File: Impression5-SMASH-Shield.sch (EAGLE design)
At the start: 113 parts, among them IC1 7805TV, J1 1725656, J10 61300811121, J11 61300811121, J12 61300611121, J13 61300311121, J14 61300311121, J15 61300311121, J16 61300311121, J17 61300311121, J18 61300311121, J19 61300611121, J2 1725656, J20 61300311121, J21 61300311121, J22 61300411121, J23 61300311121, J24 61300311121, J25 61300311121, J26 61300311121, J27 61300311121, J28 61300311121, J29 61300311121, J3 1725656, J30 61300311121, J31 61300311121, J32 61300311121, J33 61300311121, J34 61300311121, J35 61300311121, J36 61300311121, J37 61300311121, J38 61300311121, J39 61300311121, J4 1725656, J40 61300311121, J41 61300311121, J42 61300311121, J43 61300211121, J44 61300211121, J45 61300211121, J46 61300211121, J47 61300811121, J48 61300311121, J49 61300311121, J5 1725656, J50 61300311121, J51 61300311121, J52 61300611121, J53 61300811121, J54 61300811121, J6 1725656, J7 1725656, J8 1725656, J9 1725656, Q1 IRF512, Q2 IRF512, Q3 IRF512, Q4 IRF512, Q5 IRF512, Q6 IRF512, Q7 IRF512, Q8 IRF512

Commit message: Changed the Order of the Text to better line up the LM317 Programming Resistors.
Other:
- note added: "Small Vout = 3V6 R17 = 243R R16 = 453R Vout = 2.0V R19 = 243R R18 = 147R"
- note removed: "Small Vout = 2.0V R19 = 243R R18 = 147R Vout = 3V6 R17 = 243R R16 = 453R"
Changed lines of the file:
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@@
 R18 = 536R</text>
 <text x="182.88" y="73.66" size="1.778" layer="91">Small
+Vout = 3V6
+R17 = 243R
+R16 = 453R
 Vout = 2.0V
 R19 = 243R
-R18 = 147R
-Vout = 3V6
-R17 = 243R
-R16 = 453R</text>
+R18 = 147R</text>
 </plain>
 <instances>

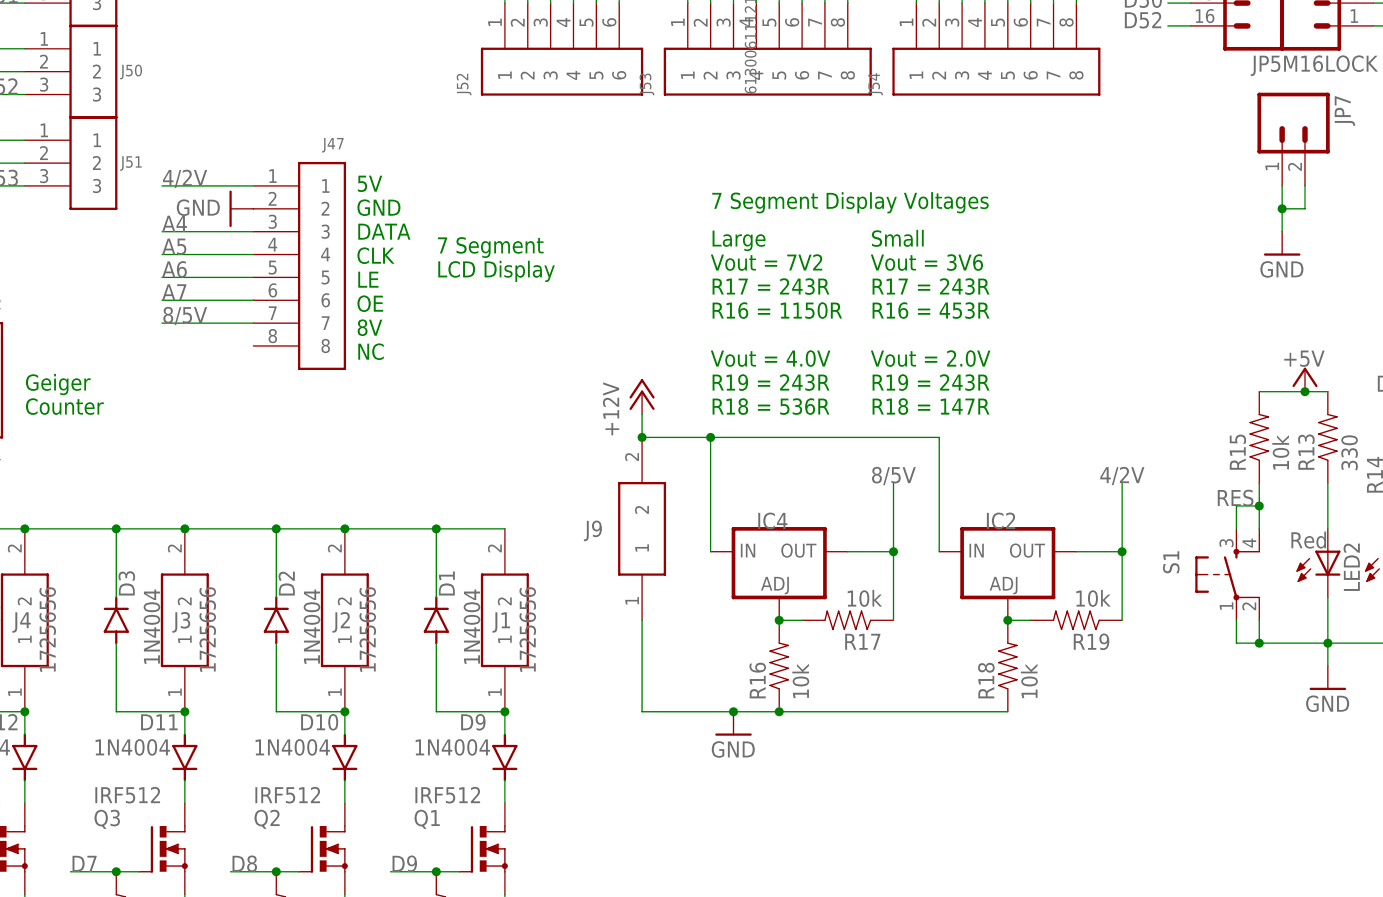
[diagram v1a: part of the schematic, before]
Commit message: changed 4/2V to 5VL. This powers the VDD of the TLC5917 and needs to be 5V.
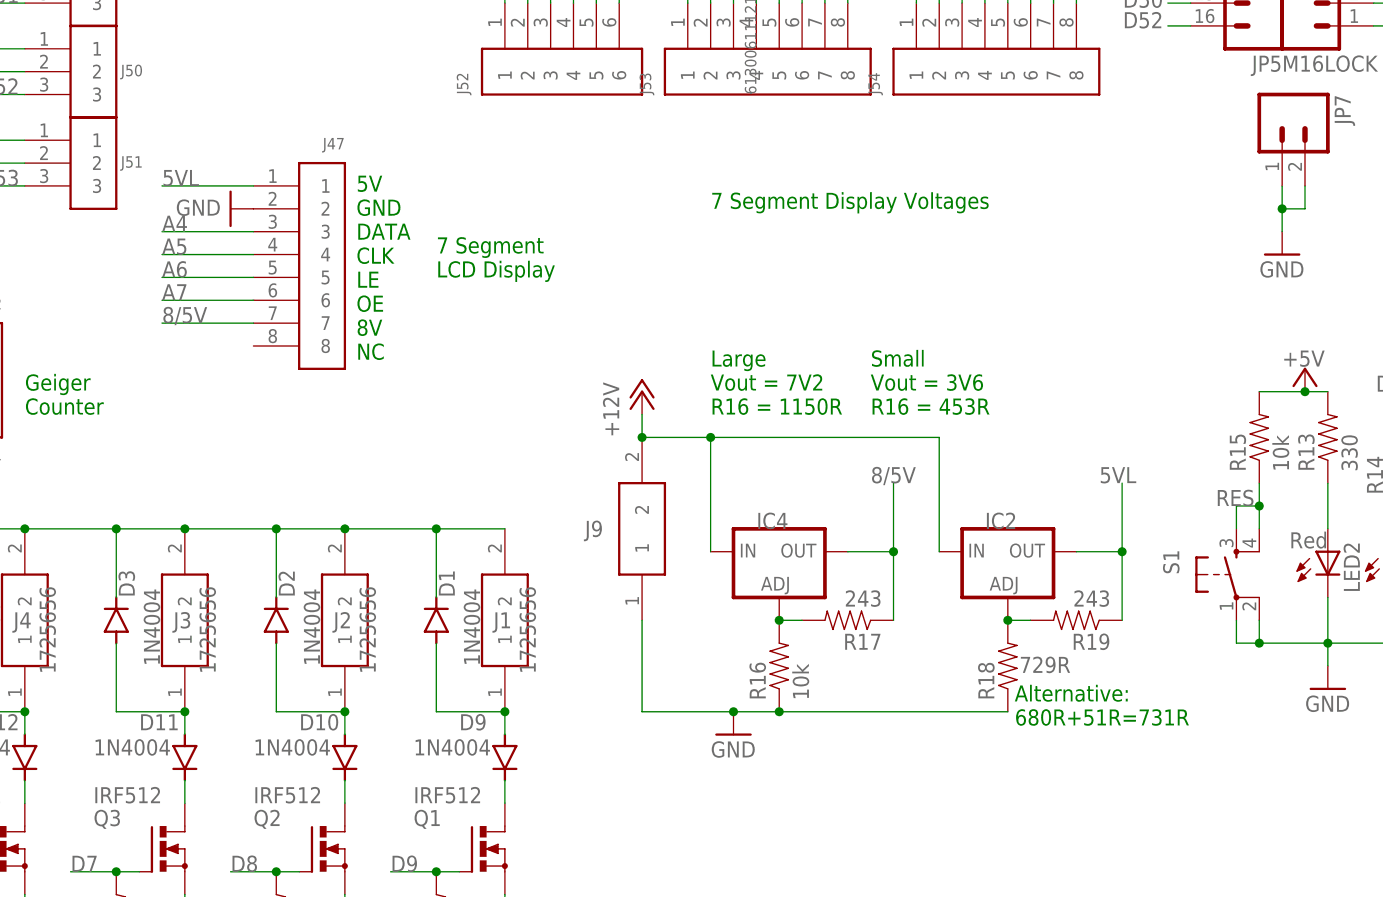
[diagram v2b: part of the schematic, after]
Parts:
- R17, R19: value 10k -> 243
- R18: value 10k -> 729R
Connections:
- net 4/2V renamed 5VL
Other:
- note added: "Alternative: 680R+51R=731R"
- note added: "Large Vout = 7V2 R16 = 1150R"
- note added: "Small Vout = 3V6 R16 = 453R"
- note removed: "Large Vout = 7V2 R17 = 243R R16 = 1150R Vout = 4.0V R19 = 243R R18 = 536R"
- note removed: "Small Vout = 3V6 R17 = 243R R16 = 453R Vout = 2.0V R19 = 243R R18 = 147R"
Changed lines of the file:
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@@
 <part name="IC4" library="v-reg" library_urn="urn:adsk.eagle:library:409" deviceset="LM317TS" device="" package3d_urn="urn:adsk.eagle:package:30353/1"/>
 <part name="R16" library="SparkFun" deviceset="RESISTOR" device="PTH1" value="10k"/>
-<part name="R17" library="SparkFun" deviceset="RESISTOR" device="PTH1" value="10k"/>
+<part name="R17" library="SparkFun" deviceset="RESISTOR" device="PTH1" value="243"/>
 <part name="IC2" library="v-reg" library_urn="urn:adsk.eagle:library:409" deviceset="LM317TS" device="" package3d_urn="urn:adsk.eagle:package:30353/1"/>
-<part name="R18" library="SparkFun" deviceset="RESISTOR" device="PTH1" value="10k"/>
-<part name="R19" library="SparkFun" deviceset="RESISTOR" device="PTH1" value="10k"/>
+<part name="R18" library="SparkFun" deviceset="RESISTOR" device="PTH1" value="729R"/>
+<part name="R19" library="SparkFun" deviceset="RESISTOR" device="PTH1" value="243"/>
 </parts>
 <sheets>
@@
 <text x="165.1" y="73.66" size="1.778" layer="91">Large
 Vout = 7V2
-R17 = 243R
-R16 = 1150R
-Vout = 4.0V
-R19 = 243R
-R18 = 536R</text>
+R16 = 1150R</text>
 <text x="182.88" y="73.66" size="1.778" layer="91">Small
 Vout = 3V6
-R17 = 243R
-R16 = 453R
-Vout = 2.0V
-R19 = 243R
-R18 = 147R</text>
+R16 = 453R</text>
+<text x="198.882" y="39.116" size="1.778" layer="91">Alternative:
+680R+51R=731R</text>
 </plain>
 <instances>
@@
 <instance part="R18" gate="G$1" x="198.12" y="45.72" smashed="yes" rot="R90">
 <attribute name="NAME" x="196.6214" y="41.91" size="1.778" layer="95" rot="R90"/>
-<attribute name="VALUE" x="201.422" y="41.91" size="1.778" layer="96" rot="R90"/>
+<attribute name="VALUE" x="199.39" y="44.958" size="1.778" layer="96"/>
 </instance>
 <instance part="R19" gate="G$1" x="205.74" y="50.8" smashed="yes" rot="R180">
@@
 </segment>
 </net>
-<net name="4/2V" class="0">
+<net name="5VL" class="0">
 <segment>
 <label x="208.28" y="66.04" size="1.778" layer="95"/>

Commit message: Changed the 8/5V to 9/5V, actually 9V2 and 5V0 respectively. These voltages needs to provide the maximum Vf that the 7-Segments may need. The max Vf are: SA23-11SRWA = 9.2V SA15-11EWA  = 5.0V
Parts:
- R16: value 10k -> 1551R or 729R
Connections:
- net 8/5V renamed 9/5V
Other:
- note added: "Alternative: 1500R+51R=1551R 680R+51R=731R"
- note added: "Large Vout = 9V2 R16 = 1551R"
- note added: "Small Vout = 5V0 R16 = 729R"
- note removed: "Large Vout = 7V2 R16 = 1150R"
- note removed: "Small Vout = 3V6 R16 = 453R"
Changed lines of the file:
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@@
 <part name="R12" library="SparkFun" deviceset="RESISTOR" device="PTH1" value="10k"/>
 <part name="IC4" library="v-reg" library_urn="urn:adsk.eagle:library:409" deviceset="LM317TS" device="" package3d_urn="urn:adsk.eagle:package:30353/1"/>
-<part name="R16" library="SparkFun" deviceset="RESISTOR" device="PTH1" value="10k"/>
+<part name="R16" library="SparkFun" deviceset="RESISTOR" device="PTH1" value="1551R or 729R"/>
 <part name="R17" library="SparkFun" deviceset="RESISTOR" device="PTH1" value="243"/>
 <part name="IC2" library="v-reg" library_urn="urn:adsk.eagle:library:409" deviceset="LM317TS" device="" package3d_urn="urn:adsk.eagle:package:30353/1"/>
@@
 <text x="165.1" y="96.52" size="1.778" layer="91">7 Segment Display Voltages</text>
 <text x="165.1" y="73.66" size="1.778" layer="91">Large
-Vout = 7V2
-R16 = 1150R</text>
+Vout = 9V2
+R16 = 1551R</text>
 <text x="182.88" y="73.66" size="1.778" layer="91">Small
-Vout = 3V6
-R16 = 453R</text>
+Vout = 5V0
+R16 = 729R</text>
 <text x="198.882" y="39.116" size="1.778" layer="91">Alternative:
+680R+51R=731R</text>
+<text x="173.736" y="33.274" size="1.778" layer="91">Alternative:
+1500R+51R=1551R
 680R+51R=731R</text>
 </plain>
@@
 <instance part="R16" gate="G$1" x="172.72" y="45.72" smashed="yes" rot="R90">
 <attribute name="NAME" x="171.2214" y="41.91" size="1.778" layer="95" rot="R90"/>
-<attribute name="VALUE" x="176.022" y="41.91" size="1.778" layer="96" rot="R90"/>
+<attribute name="VALUE" x="173.99" y="42.418" size="1.778" layer="96"/>
 </instance>
 <instance part="R17" gate="G$1" x="180.34" y="50.8" smashed="yes" rot="R180">
@@
 </segment>
 </net>
-<net name="8/5V" class="0">
+<net name="9/5V" class="0">
 <segment>
 <label x="182.88" y="66.04" size="1.778" layer="95"/>

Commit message: Added Notes for double use of D2 and D9
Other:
- note added: "Note - D2 is used in TWO places, on J8 Mosfet control and Geiger Counter Pulse Interupt D9 is used in TWO places, on J1 Mosfet control and Relay Board control"
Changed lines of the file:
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@@
 <text x="88.9" y="73.66" size="1.778" layer="91">Geiger
 Counter</text>
-<text x="165.1" y="96.52" size="1.778" layer="91">7 Segment Display Voltages</text>
+<text x="160.02" y="81.28" size="1.778" layer="91">7 Segment Display Voltages</text>
 <text x="165.1" y="73.66" size="1.778" layer="91">Large
 Vout = 9V2
@@
 1500R+51R=1551R
 680R+51R=731R</text>
+<wire x1="2.54" y1="25.4" x2="2.54" y2="21.59" width="0.1524" layer="101"/>
+<wire x1="2.54" y1="21.59" x2="9.144" y2="21.59" width="0.1524" layer="101"/>
+<wire x1="9.144" y1="21.59" x2="9.144" y2="25.4" width="0.1524" layer="101"/>
+<wire x1="9.144" y1="25.4" x2="2.54" y2="25.4" width="0.1524" layer="101"/>
+<wire x1="70.358" y1="75.692" x2="70.358" y2="72.644" width="0.1524" layer="101"/>
+<wire x1="70.358" y1="72.644" x2="75.692" y2="72.644" width="0.1524" layer="101"/>
+<wire x1="75.692" y1="72.644" x2="75.692" y2="75.692" width="0.1524" layer="101"/>
+<wire x1="75.692" y1="75.692" x2="70.358" y2="75.692" width="0.1524" layer="101"/>
+<wire x1="11.684" y1="85.852" x2="11.684" y2="83.312" width="0.1524" layer="101"/>
+<wire x1="11.684" y1="83.312" x2="6.858" y2="83.312" width="0.1524" layer="101"/>
+<wire x1="6.858" y1="83.312" x2="6.858" y2="85.852" width="0.1524" layer="101"/>
+<wire x1="6.858" y1="85.852" x2="11.684" y2="85.852" width="0.1524" layer="101"/>
+<wire x1="133.096" y1="25.146" x2="133.096" y2="22.098" width="0.1524" layer="101"/>
+<wire x1="133.096" y1="22.098" x2="129.032" y2="22.098" width="0.1524" layer="101"/>
+<wire x1="129.032" y1="22.098" x2="129.032" y2="25.146" width="0.1524" layer="101"/>
+<wire x1="129.032" y1="25.146" x2="133.096" y2="25.146" width="0.1524" layer="101"/>
+<text x="149.86" y="27.94" size="1.778" layer="101">Note -
+D2 is used in TWO places, on J8 Mosfet control and Geiger Counter Pulse Interupt
+D9 is used in TWO places, on J1 Mosfet control and Relay Board control</text>
 </plain>
 <instances>
